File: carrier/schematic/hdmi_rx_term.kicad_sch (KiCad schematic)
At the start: 8 parts

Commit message: genpolish: TITLE-1 — populate the schematic title block on every sheet
Every sheet rendered a blank Title/Rev/Date — the clearest 'not a real
schematic' tell. emit() now writes a (title_block ...) after the paper node:
title = the sheet circuit's title, company "Zynq SoM Carrier", and a
"<sheet> — generated by schgen (do not hand-edit)" comment. NO date node — a
wall-clock date would break byte-determinism; the content-derived fields keep
every rebuild identical. Verified on A4 (usb_pd) and the dense A3 (power): the
block fills the standard reserved corner with zero drawing overlap. All 26
sheets, goldens re-blessed, board PASS + deterministic, selftest 53/53, m1,
pytest 147.

Co-Authored-By: Claude Opus 4.8 <noreply@anthropic.com>
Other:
- company: (none) -> Zynq SoM Carrier
- title: (none) -> HDMI-RX TMDS sink termination (8x49.9R to AVCC=+3V3)
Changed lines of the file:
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@@
 	(generator_version "1.0")
 	(paper "A4")
+	(title_block
+		(title "HDMI-RX TMDS sink termination (8x49.9R to AVCC=+3V3)")
+		(company "Zynq SoM Carrier")
+		(comment 1 "hdmi_rx_term — generated by schgen (do not hand-edit)")
+	)
 	(wire
 		(pts

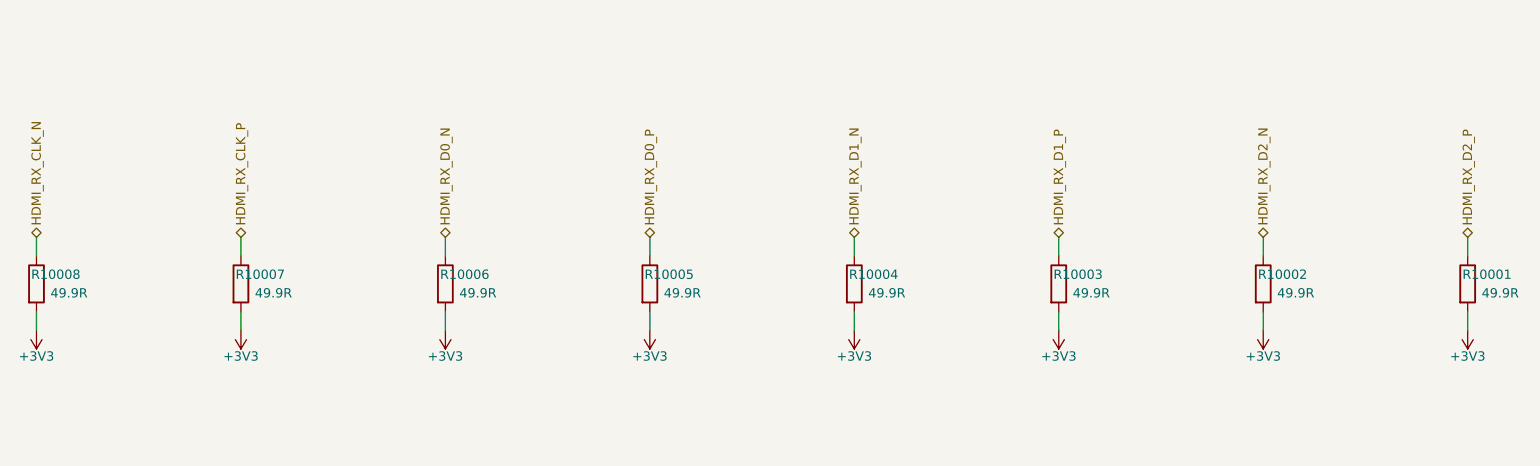
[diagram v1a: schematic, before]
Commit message: board: four board-management HW blocks on a manually-gated +3V3_AUX (BOARDHW)
The four services the carrier was missing — all behind ONE manual power enable
(C1) on two new sheets split so neither defeats the placer's rail-stub router:

  board_aux       — the gate + I2C isolator (infrastructure)
  board_services  — ID-EEPROM + RTC + watchdog + QWIIC (the peripherals)

WHAT LANDED
  * 24AA025E48 (C129895)  ID-EEPROM with a factory EUI-48 **MAC** for the
      LAN8720/RJ45 — strapped 0x51 (0x50 is the FMC EEPROM).
  * RV-3028-C7 (C3019759) I2C RTC, integrated DTCXO (no crystal), CR1220 coin
      cell (KH-CR1220-2) with auto-switchover, 0x52.
  * TPS3823-33 (C7719)    supervisor + windowed watchdog.
  * ZX-SH1.0-4PWT (C7430446)  QWIIC / STEMMA-QT expansion (gated 3V3 + the
      isolated AUX I2C).
  * SY6280 gate + DSHP04 DIP + PCA9306 isolator complete the infrastructure.

CONSTRAINTS (the user's three standing requirements)
  C1 manual enable "like the previous": +3V3_AUX is a SY6280 load switch whose
     EN is a default-OFF DSHP04 DIP (100k pulldown) — the same gated-module
     idiom, self-contained so it touches none of the dense rail/EN sheets.
  C2 "no watchdog reset during power-up": THREE independent guards — (1) the
     supervisor's VDD is the default-OFF +3V3_AUX, so it is UNPOWERED through
     power-up; (2) the TPS3823 disables its watchdog while WDI floats, and WDI
     is driven only by the PL (WATCHDOG_KICK, Hi-Z until the fabric is up); (3)
     RESET# is a firmware-mediated PL EVENT (J3.31), never a rail/POR line.
  C3 Zynq-agnostic: the only SoM-side signals (the 2 watchdog lines) ride PL
     bank-35 IO by their contract net names (IO_L16_N/P_35 -> J3.29/31); xdc.py
     emits the constraints live — nothing hard-codes the Zynq part.

LAW 0 (electrical integrity): the peripherals sit on the GATED rail but their
bus is the always-on STM32_I2C2 management bus. A PCA9306 bridges them with EN
tied to +3V3_AUX, so the switch OPENS whenever the rail is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
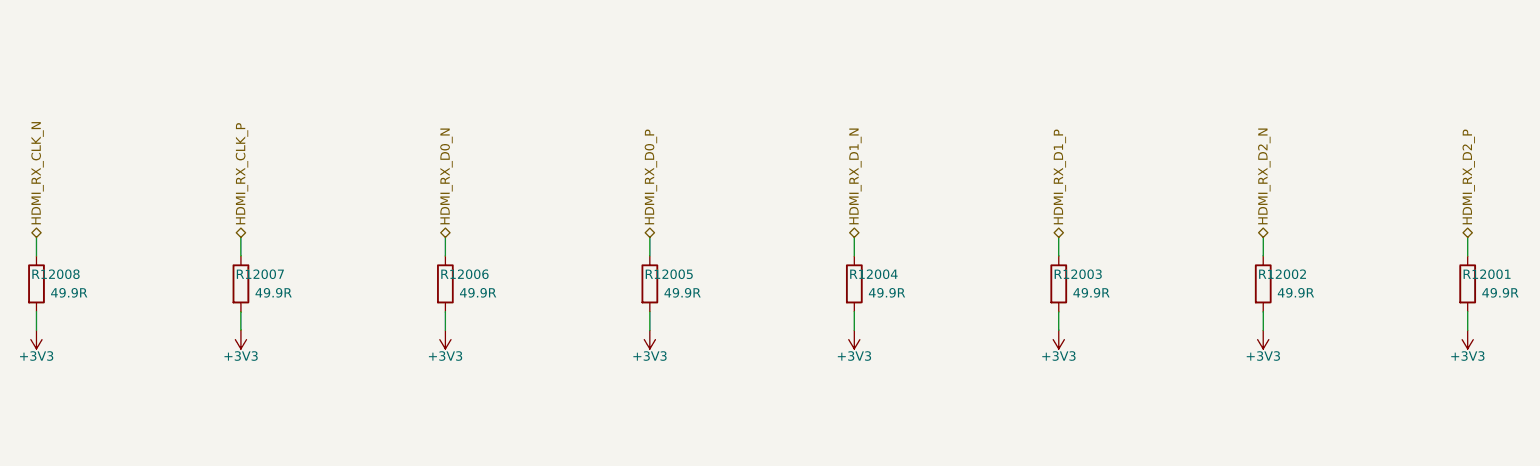
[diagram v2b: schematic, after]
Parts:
- renumbered R10001 to R12001, R10002 to R12002, R10003 to R12003, R10004 to R12004, R10005 to R12005, R10006 to R12006, R10007 to R12007, R10008 to R12008
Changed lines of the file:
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@@
 		(property
 			"Reference"
-			"R10008"
+			"R12008"
 			(at 50.902 99.06 0)
 			(effects
@@
 				(path
 					"/c2797150-7a6e-556a-82f5-fdda13c31368/8a423326-7c89-5fe5-8f98-7d26b0d81668"
-					(reference "R10008")
+					(reference "R12008")
 					(unit 1)
 				)
@@
 		(property
 			"Reference"
-			"R10007"
+			"R12007"
 			(at 78.843 99.06 0)
 			(effects
@@
 				(path
 					"/c2797150-7a6e-556a-82f5-fdda13c31368/8a423326-7c89-5fe5-8f98-7d26b0d81668"
-					(reference "R10007")
+					(reference "R12007")
 					(unit 1)
 				)
@@
 		(property
 			"Reference"
-			"R10006"
+			"R12006"
 			(at 106.782 99.06 0)
 			(effects
@@
 				(path
 					"/c2797150-7a6e-556a-82f5-fdda13c31368/8a423326-7c89-5fe5-8f98-7d26b0d81668"
-					(reference "R10006")
+					(reference "R12006")
 					(unit 1)
 				)
@@
 		(property
 			"Reference"
-			"R10005"
+			"R12005"
 			(at 134.722 99.06 0)
 			(effects
@@
 				(path
 					"/c2797150-7a6e-556a-82f5-fdda13c31368/8a423326-7c89-5fe5-8f98-7d26b0d81668"
-					(reference "R10005")
+					(reference "R12005")
 					(unit 1)
 				)
@@
 		(property
 			"Reference"
-			"R10004"
+			"R12004"
 			(at 162.662 99.06 0)
 			(effects
@@
 				(path
 					"/c2797150-7a6e-556a-82f5-fdda13c31368/8a423326-7c89-5fe5-8f98-7d26b0d81668"
-					(reference "R10004")
+					(reference "R12004")
 					(unit 1)
 				)
@@
 		(property
 			"Reference"
-			"R10003"
+			"R12003"
 			(at 190.602 99.06 0)
 			(effects
@@
 				(path
 					"/c2797150-7a6e-556a-82f5-fdda13c31368/8a423326-7c89-5fe5-8f98-7d26b0d81668"
-					(reference "R10003")
+					(reference "R12003")
 					(unit 1)
 				)
@@
 		(property
 			"Reference"
-			"R10002"
+			"R12002"
 			(at 218.542 99.06 0)
 			(effects
@@
 				(path
 					"/c2797150-7a6e-556a-82f5-fdda13c31368/8a423326-7c89-5fe5-8f98-7d26b0d81668"
-					(reference "R10002")
+					(reference "R12002")
 					(unit 1)
 				)
@@
 		(property
 			"Reference"
-			"R10001"
+			"R12001"
 			(at 246.482 99.06 0)
 			(effects
@@
 				(path
 					"/c2797150-7a6e-556a-82f5-fdda13c31368/8a423326-7c89-5fe5-8f98-7d26b0d81668"
-					(reference "R10001")
+					(reference "R12001")
 					(unit 1)
 				)
@@
 		(property
 			"Reference"
-			"#PWR10001"
+			"#PWR12001"
 			(at 48.26 104.14 0)
 			(effects
@@
 				(path
 					"/c2797150-7a6e-556a-82f5-fdda13c31368/8a423326-7c89-5fe5-8f98-7d26b0d81668"
-					(reference "#PWR10001")
+					(reference "#PWR12001")
 					(unit 1)
 				)
@@
 		(property
 			"Reference"
-			"#PWR10002"
+			"#PWR12002"
 			(at 76.2 104.14 0)
 			(effects
@@
 				(path
 					"/c2797150-7a6e-556a-82f5-fdda13c31368/8a423326-7c89-5fe5-8f98-7d26b0d81668"
-					(reference "#PWR10002")
+					(reference "#PWR12002")
 					(unit 1)
 				)
@@
 		(property
 			"Reference"
-			"#PWR10003"
+			"#PWR12003"
 			(at 104.14 104.14 0)
 			(effects
@@
 				(path
 					"/c2797150-7a6e-556a-82f5-fdda13c31368/8a423326-7c89-5fe5-8f98-7d26b0d81668"
-					(reference "#PWR10003")
+					(reference "#PWR12003")
 					(unit 1)
 				)
@@
 		(property
 			"Reference"
-			"#PWR10004"
+			"#PWR12004"
 			(at 132.08 104.14 0)
 			(effects
@@
 				(path
 					"/c2797150-7a6e-556a-82f5-fdda13c31368/8a423326-7c89-5fe5-8f98-7d26b0d81668"
-					(reference "#PWR10004")
+					(reference "#PWR12004")
 					(unit 1)
 				)
@@
 		(property
 			"Reference"
-			"#PWR10005"
+			"#PWR12005"
 			(at 160.02 104.14 0)
 			(effects
@@
 				(path
 					"/c2797150-7a6e-556a-82f5-fdda13c31368/8a423326-7c89-5fe5-8f98-7d26b0d81668"
-					(reference "#PWR10005")
+					(reference "#PWR12005")
 					(unit 1)
 				)
@@
 		(property
 			"Reference"
-			"#PWR10006"
+			"#PWR12006"
 			(at 187.96 104.14 0)
 			(effects
@@
 				(path
 					"/c2797150-7a6e-556a-82f5-fdda13c31368/8a423326-7c89-5fe5-8f98-7d26b0d81668"
-					(reference "#PWR10006")
+					(reference "#PWR12006")
 					(unit 1)
 				)
@@
 		(property
 			"Reference"
-			"#PWR10007"
+			"#PWR12007"
 			(at 215.9 104.14 0)
 			(effects
@@
 				(path
 					"/c2797150-7a6e-556a-82f5-fdda13c31368/8a423326-7c89-5fe5-8f98-7d26b0d81668"
-					(reference "#PWR10007")
+					(reference "#PWR12007")
 					(unit 1)
 				)
@@
 		(property
 			"Reference"
-			"#PWR10008"
+			"#PWR12008"
 			(at 243.84 104.14 0)
 			(effects
@@
 				(path
 					"/c2797150-7a6e-556a-82f5-fdda13c31368/8a423326-7c89-5fe5-8f98-7d26b0d81668"
-					(reference "#PWR10008")
-					(unit 1)
-				)
+					(reference "#PWR12008")
+					(unit 1)
+				)

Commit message: audit fixes: QWIIC ESD on its own sheet + firmware I2C-map completeness
Acting on a multi-agent adversarial re-audit of the 28-sheet board. Each
finding was independently re-verified before action — two confident "HIGH"
findings were FALSE POSITIVES whose proposed fixes would have INTRODUCED bugs,
and are documented-rejected, not applied:

  * "DSHP04 switches in parallel" — wrong. The footprint pads prove the pairing
    by physical opposition (switch n = pads n & 9-n): switch 1 = pads 1&8 is the
    only one on EN_AUX; the other even pins (2/4/6) are NC, identical to the
    proven bringup_rails SW6 idiom. The proposed "fix" (pins 1+2) wires two
    DIFFERENT switches and would leave EN_AUX permanently pulled down — the rail
    could never enable.
  * "PCA9306 EN floats when AUX is off" — wrong. A 100k to a 0 V rail pulls EN
    to 0 V (disabled), which is exactly TI's recommended "isolate when the gated
    side is unpowered" connection. No float.

REAL findings actioned:

1. QWIIC connector lacked ESD (every other external connector has it). Moved the
   QWIIC out of board_services onto its own sheet board_qwiic (the carrier's
   connectors-get-their-own-sheet idiom — rj45_connector, usb_uart_connector)
   and added a USBLC6-2SC6 low-cap ESD array at the connector (1<->6 / 3<->4
   passthrough, clamp ref +3V3_AUX). The dedicated sheet also keeps both sheets
   sparse enough for the rail-stub router. board_services drops to 9 parts.

2. schgen/firmware.py loaded only 7 sheets, so the SC-firmware contract + its
   I2C address-collision check were BLIND to the new devices. Added board_aux/
   board_services to SOURCES and three address rows: FMC-EEPROM 0x50, ID-EEPROM
   0x51 (DERIVED from the 24AA025E48 A1/A0 straps, so a mis-strap to 0x50 now
   trips the collision check against the FMC EEPROM), RTC 0x52. The firmware can
   now address the EUI-48 MAC EEPROM and the RTC. 114 -> 117 #defines.

3. board_services docstring clarified (EEPROM/RTC are on the PCA9306-i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
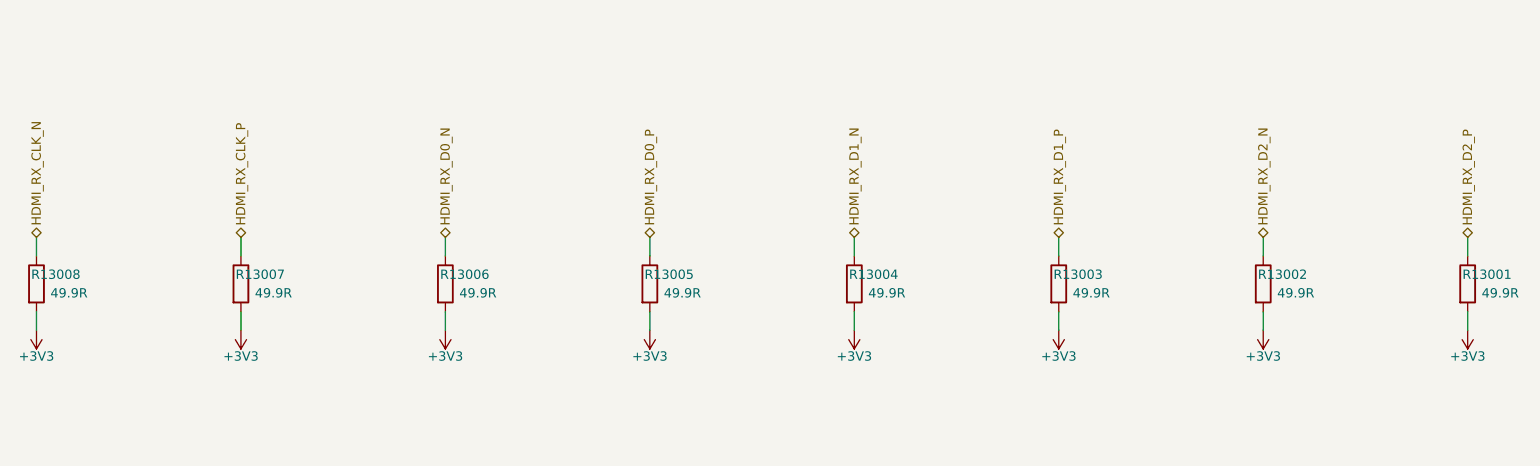
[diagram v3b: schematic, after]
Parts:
- renumbered R12001 to R13001, R12002 to R13002, R12003 to R13003, R12004 to R13004, R12005 to R13005, R12006 to R13006, R12007 to R13007, R12008 to R13008
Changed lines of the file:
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@@
 		(property
 			"Reference"
-			"R12008"
+			"R13008"
 			(at 50.902 99.06 0)
 			(effects
@@
 				(path
 					"/c2797150-7a6e-556a-82f5-fdda13c31368/8a423326-7c89-5fe5-8f98-7d26b0d81668"
-					(reference "R12008")
+					(reference "R13008")
 					(unit 1)
 				)
@@
 		(property
 			"Reference"
-			"R12007"
+			"R13007"
 			(at 78.843 99.06 0)
 			(effects
@@
 				(path
 					"/c2797150-7a6e-556a-82f5-fdda13c31368/8a423326-7c89-5fe5-8f98-7d26b0d81668"
-					(reference "R12007")
+					(reference "R13007")
 					(unit 1)
 				)
@@
 		(property
 			"Reference"
-			"R12006"
+			"R13006"
 			(at 106.782 99.06 0)
 			(effects
@@
 				(path
 					"/c2797150-7a6e-556a-82f5-fdda13c31368/8a423326-7c89-5fe5-8f98-7d26b0d81668"
-					(reference "R12006")
+					(reference "R13006")
 					(unit 1)
 				)
@@
 		(property
 			"Reference"
-			"R12005"
+			"R13005"
 			(at 134.722 99.06 0)
 			(effects
@@
 				(path
 					"/c2797150-7a6e-556a-82f5-fdda13c31368/8a423326-7c89-5fe5-8f98-7d26b0d81668"
-					(reference "R12005")
+					(reference "R13005")
 					(unit 1)
 				)
@@
 		(property
 			"Reference"
-			"R12004"
+			"R13004"
 			(at 162.662 99.06 0)
 			(effects
@@
 				(path
 					"/c2797150-7a6e-556a-82f5-fdda13c31368/8a423326-7c89-5fe5-8f98-7d26b0d81668"
-					(reference "R12004")
+					(reference "R13004")
 					(unit 1)
 				)
@@
 		(property
 			"Reference"
-			"R12003"
+			"R13003"
 			(at 190.602 99.06 0)
 			(effects
@@
 				(path
 					"/c2797150-7a6e-556a-82f5-fdda13c31368/8a423326-7c89-5fe5-8f98-7d26b0d81668"
-					(reference "R12003")
+					(reference "R13003")
 					(unit 1)
 				)
@@
 		(property
 			"Reference"
-			"R12002"
+			"R13002"
 			(at 218.542 99.06 0)
 			(effects
@@
 				(path
 					"/c2797150-7a6e-556a-82f5-fdda13c31368/8a423326-7c89-5fe5-8f98-7d26b0d81668"
-					(reference "R12002")
+					(reference "R13002")
 					(unit 1)
 				)
@@
 		(property
 			"Reference"
-			"R12001"
+			"R13001"
 			(at 246.482 99.06 0)
 			(effects
@@
 				(path
 					"/c2797150-7a6e-556a-82f5-fdda13c31368/8a423326-7c89-5fe5-8f98-7d26b0d81668"
-					(reference "R12001")
+					(reference "R13001")
 					(unit 1)
 				)
@@
 		(property
 			"Reference"
-			"#PWR12001"
+			"#PWR13001"
 			(at 48.26 104.14 0)
 			(effects
@@
 				(path
 					"/c2797150-7a6e-556a-82f5-fdda13c31368/8a423326-7c89-5fe5-8f98-7d26b0d81668"
-					(reference "#PWR12001")
+					(reference "#PWR13001")
 					(unit 1)
 				)
@@
 		(property
 			"Reference"
-			"#PWR12002"
+			"#PWR13002"
 			(at 76.2 104.14 0)
 			(effects
@@
 				(path
 					"/c2797150-7a6e-556a-82f5-fdda13c31368/8a423326-7c89-5fe5-8f98-7d26b0d81668"
-					(reference "#PWR12002")
+					(reference "#PWR13002")
 					(unit 1)
 				)
@@
 		(property
 			"Reference"
-			"#PWR12003"
+			"#PWR13003"
 			(at 104.14 104.14 0)
 			(effects
@@
 				(path
 					"/c2797150-7a6e-556a-82f5-fdda13c31368/8a423326-7c89-5fe5-8f98-7d26b0d81668"
-					(reference "#PWR12003")
+					(reference "#PWR13003")
 					(unit 1)
 				)
@@
 		(property
 			"Reference"
-			"#PWR12004"
+			"#PWR13004"
 			(at 132.08 104.14 0)
 			(effects
@@
 				(path
 					"/c2797150-7a6e-556a-82f5-fdda13c31368/8a423326-7c89-5fe5-8f98-7d26b0d81668"
-					(reference "#PWR12004")
+					(reference "#PWR13004")
 					(unit 1)
 				)
@@
 		(property
 			"Reference"
-			"#PWR12005"
+			"#PWR13005"
 			(at 160.02 104.14 0)
 			(effects
@@
 				(path
 					"/c2797150-7a6e-556a-82f5-fdda13c31368/8a423326-7c89-5fe5-8f98-7d26b0d81668"
-					(reference "#PWR12005")
+					(reference "#PWR13005")
 					(unit 1)
 				)
@@
 		(property
 			"Reference"
-			"#PWR12006"
+			"#PWR13006"
 			(at 187.96 104.14 0)
 			(effects
@@
 				(path
 					"/c2797150-7a6e-556a-82f5-fdda13c31368/8a423326-7c89-5fe5-8f98-7d26b0d81668"
-					(reference "#PWR12006")
+					(reference "#PWR13006")
 					(unit 1)
 				)
@@
 		(property
 			"Reference"
-			"#PWR12007"
+			"#PWR13007"
 			(at 215.9 104.14 0)
 			(effects
@@
 				(path
 					"/c2797150-7a6e-556a-82f5-fdda13c31368/8a423326-7c89-5fe5-8f98-7d26b0d81668"
-					(reference "#PWR12007")
+					(reference "#PWR13007")
 					(unit 1)
 				)
@@
 		(property
 			"Reference"
-			"#PWR12008"
+			"#PWR13008"
 			(at 243.84 104.14 0)
 			(effects
@@
 				(path
 					"/c2797150-7a6e-556a-82f5-fdda13c31368/8a423326-7c89-5fe5-8f98-7d26b0d81668"
-					(reference "#PWR12008")
-					(unit 1)
-				)
+					(reference "#PWR13008")
+					(unit 1)
+				)

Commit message: carrier: regen artifacts — DEF-G HDMI-RX TMDS ESD arrays + AVCC bypass
Co-Authored-By: Claude Opus 4.8 <noreply@anthropic.com>
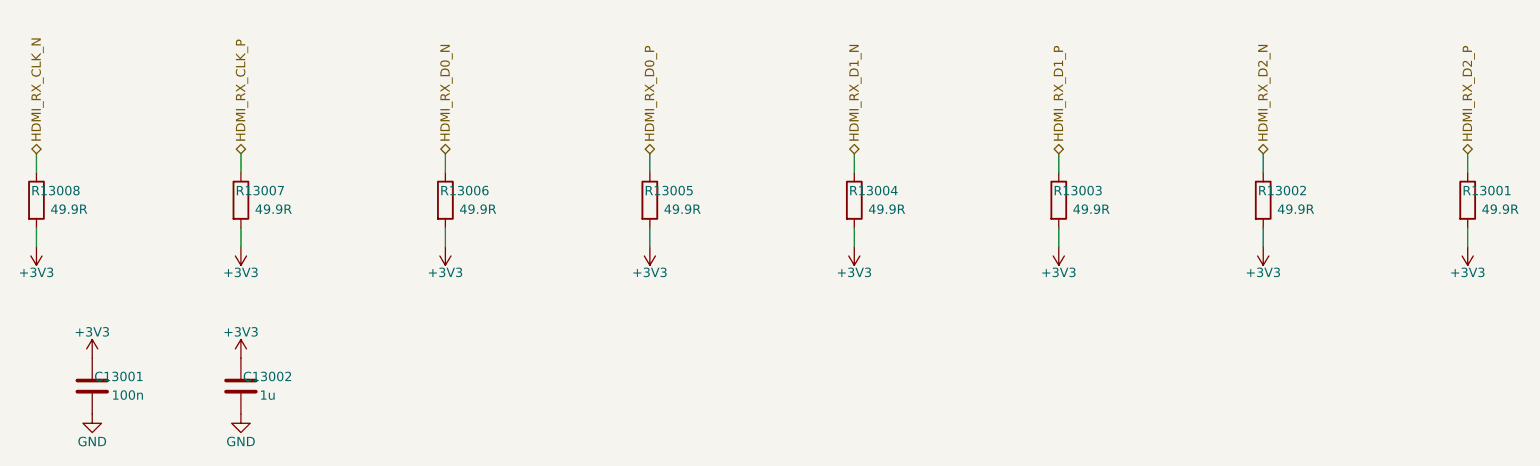
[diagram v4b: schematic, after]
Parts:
- added C13001: 100n, Capacitor_SMD:C_0603_1608Metric, symbol Device:C
- added C13002: 1u, Capacitor_SMD:C_0603_1608Metric, symbol Device:C
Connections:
- net +3V3: now also C13001.1, C13002.1
- new net GND: C13001.2, C13002.2
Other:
- moved on the sheet: R13001, R13002, R13003, R13004, R13005, R13006, R13007, R13008
